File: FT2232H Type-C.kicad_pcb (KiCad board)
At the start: 2 copper layers, 52 x 40 mm, 34 parts, among them J1 CONN_01X20, J2 CONN_01X20, J3 USB_TYPE_C, U1 LD1117S33TR, U3 93CxxB, U4 FT2232H, Y1 12Mhz

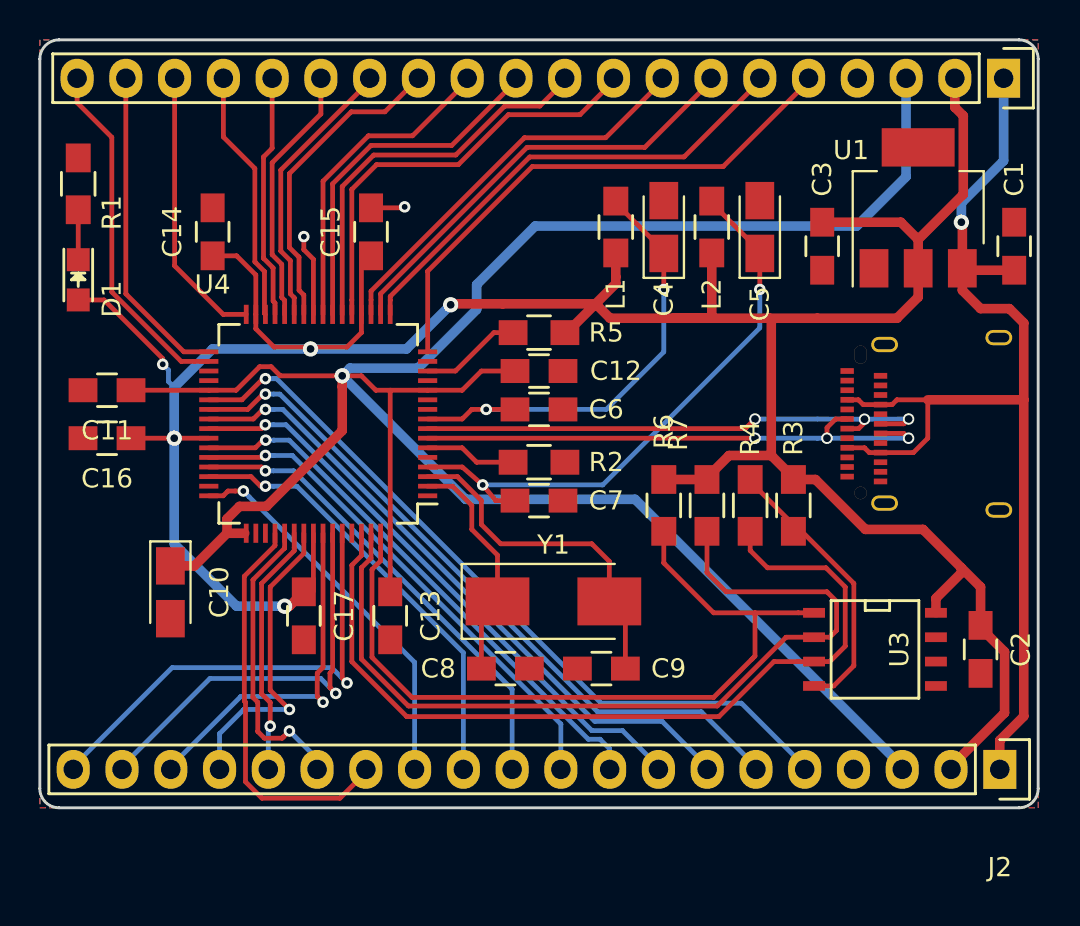
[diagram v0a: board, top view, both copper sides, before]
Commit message: Add silkscreen
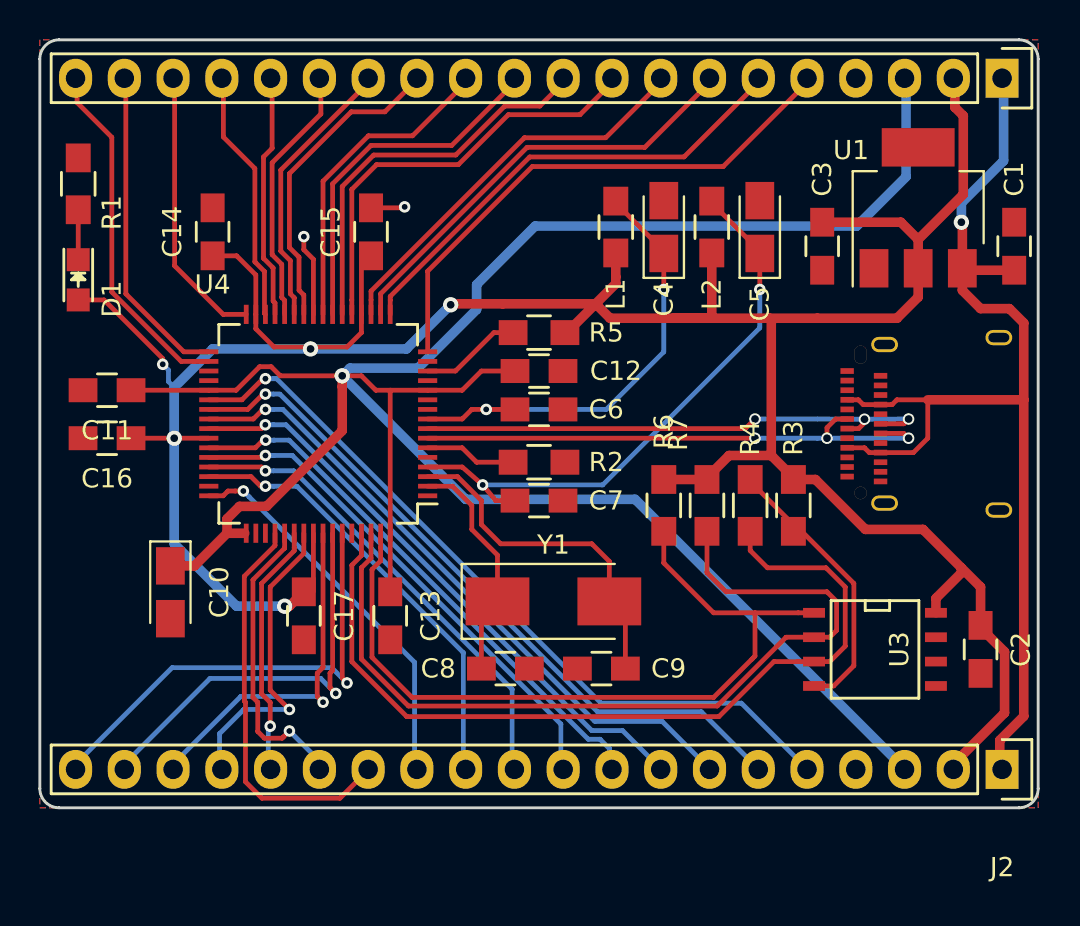
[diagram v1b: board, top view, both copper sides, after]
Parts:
- moved J2 0.12 mm to (198.1, 118.0)
- moved J1 0.08 mm to (198.1, 82.0)
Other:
- rule pad_to_mask_clearance: 0.2 -> 0.1
- board text added: "1.8V"
- board text added: "3.3V"
- board text added: "5.0V"
- board text added: "AC0"
- board text added: "AC1"
- board text added: "AC2"
- board text added: "AC3"
- board text added: "AC4"
- board text added: "AC5"
- board text added: "AC6"
- board text added: "AC7"
- board text added: "AD0"
- board text added: "AD1"
- board text added: "AD2"
- board text added: "AD3"
- board text added: "AD4"
- board text added: "AD5"
- board text added: "AD6"
- board text added: "AD7"
- board text added: "BC0"
- board text added: "BC1"
- board text added: "BC2"
- board text added: "BC3"
- board text added: "BC4"
- board text added: "BC5"
- board text added: "BC6"
- board text added: "BC7"
- board text added: "BD0"
- board text added: "BD1"
- board text added: "BD2"
- board text added: "BD3"
- board text added: "BD4"
- board text added: "BD5"
- board text added: "BD6"
- board text added: "BD7"
- board text added: "FT2232H Type-C Breakout Board Charles-Xavier Roy, Aug 2017"
- board text added: "GND"
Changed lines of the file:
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@@
   (general
     (links 130)
-    (no_connects 64)
+    (no_connects 40)
     (area 147.924999 79.924999 200.075001 120.075001)
     (thickness 1.6)
-    (drawings 8)
+    (drawings 49)
     (tracks 516)
     (zones 0)
@@
     (pad_size 1.524 1.524)
     (pad_drill 0.762)
-    (pad_to_mask_clearance 0.2)
+    (pad_to_mask_clearance 0.1)
+    (solder_mask_min_width 0.32)
     (aux_axis_origin 0 0)
     (visible_elements FFFFFF7F)
     (pcbplotparams
-      (layerselection 0x00030_80000001)
+      (layerselection 0x010f0_80000001)
       (usegerberextensions false)
       (excludeedgelayer true)
@@
       (outputformat 1)
       (mirror false)
-      (drillshape 1)
+      (drillshape 0)
       (scaleselection 1)
-      (outputdirectory ""))
+      (outputdirectory build/))
   )
   (net 0 "")
@@
   )
   (module Socket_Strips:Socket_Strip_Straight_1x20 (layer F.Cu)
-    (at 198.2 82 180)
+    (at 198.12 82 180)
     (descr "Through hole socket strip")
     (tags "socket strip")
@@
   )
   (module Socket_Strips:Socket_Strip_Straight_1x20 (layer F.Cu)
-    (at 198 118 180)
+    (at 198.12 118 180)
     (descr "Through hole socket strip")
     (tags "socket strip")
@@
     )
   )
+  (gr_text "FT2232H Type-C Breakout Board\nCharles-Xavier Roy, Aug 2017" (at 173.75 100.25) (layer B.SilkS)
+    (effects (font (size 1.5 1.5) (thickness 0.3)) (justify mirror))
+  )
+  (gr_text AC0 (at 167.64 83.82 270) (layer B.SilkS)
+    (effects (font (size 1.5 1.5) (thickness 0.3)) (justify right mirror))
+  )
+  (gr_text AD6 (at 172.72 83.82 270) (layer B.SilkS)
+    (effects (font (size 1.5 1.5) (thickness 0.3)) (justify right mirror))
+  )
+  (gr_text AD7 (at 170.18 83.82 270) (layer B.SilkS)
+    (effects (font (size 1.5 1.5) (thickness 0.3)) (justify right mirror))
+  )
+  (gr_text AD4 (at 177.8 83.82 270) (layer B.SilkS)
+    (effects (font (size 1.5 1.5) (thickness 0.3)) (justify right mirror))
+  )
+  (gr_text AD3 (at 180.34 83.82 270) (layer B.SilkS)
+    (effects (font (size 1.5 1.5) (thickness 0.3)) (justify right mirror))
+  )
+  (gr_text AD5 (at 175.26 83.82 270) (layer B.SilkS)
+    (effects (font (size 1.5 1.5) (thickness 0.3)) (justify right mirror))
+  )
+  (gr_text AC7 (at 149.86 83.82 270) (layer B.SilkS)
+    (effects (font (size 1.5 1.5) (thickness 0.3)) (justify right mirror))
+  )
+  (gr_text AC5 (at 154.94 83.82 270) (layer B.SilkS)
+    (effects (font (size 1.5 1.5) (thickness 0.3)) (justify right mirror))
+  )
+  (gr_text AC6 (at 152.4 83.82 270) (layer B.SilkS)
+    (effects (font (size 1.5 1.5) (thickness 0.3)) (justify right mirror))
+  )
+  (gr_text AC1 (at 165.1 83.82 270) (layer B.SilkS)
+    (effects (font (size 1.5 1.5) (thickness 0.3)) (justify right mirror))
+  )
+  (gr_text AC2 (at 162.56 83.82 270) (layer B.SilkS)
+    (effects (font (size 1.5 1.5) (thickness 0.3)) (justify right mirror))
+  )
+  (gr_text AC3 (at 160.02 83.82 270) (layer B.SilkS)
+    (effects (font (size 1.5 1.5) (thickness 0.3)) (justify right mirror))
+  )
+  (gr_text AC4 (at 157.48 83.82 270) (layer B.SilkS)
+    (effects (font (size 1.5 1.5) (thickness 0.3)) (justify right mirror))
+  )
+  (gr_text 5.0V (at 198.12 83.82 270) (layer B.SilkS)
+    (effects (font (size 1.5 1.5) (thickness 0.3)) (justify right mirror))
+  )
+  (gr_text GND (at 190.5 83.82 270) (layer B.SilkS)
+    (effects (font (size 1.5 1.5) (thickness 0.3)) (justify right mirror))
+  )
+  (gr_text AD0 (at 187.96 83.82 270) (layer B.SilkS)
+    (effects (font (size 1.5 1.5) (thickness 0.3)) (justify right mirror))
+  )
+  (gr_text AD2 (at 182.88 83.82 270) (layer B.SilkS)
+    (effects (font (size 1.5 1.5) (thickness 0.3)) (justify right mirror))
+  )
+  (gr_text AD1 (at 185.42 83.82 270) (layer B.SilkS)
+    (effects (font (size 1.5 1.5) (thickness 0.3)) (justify right mirror))
+  )
+  (gr_text 1.8V (at 193.04 83.82 270) (layer B.SilkS)
+    (effects (font (size 1.5 1.5) (thickness 0.3)) (justify right mirror))
+  )
+  (gr_text 3.3V (at 195.58 83.82 270) (layer B.SilkS)
+    (effects (font (size 1.5 1.5) (thickness 0.3)) (justify right mirror))
+  )
+  (gr_text 5.0V (at 198.12 116.34 270) (layer B.SilkS)
+    (effects (font (size 1.5 1.5) (thickness 0.3)) (justify left mirror))
+  )
+  (gr_text 3.3V (at 195.58 116.34 270) (layer B.SilkS)
+    (effects (font (size 1.5 1.5) (thickness 0.3)) (justify left mirror))
+  )
+  (gr_text 1.8V (at 193.04 116.34 270) (layer B.SilkS)
+    (effects (font (size 1.5 1.5) (thickness 0.3)) (justify left mirror))
+  )
+  (gr_text GND (at 190.5 116.34 270) (layer B.SilkS)
+    (effects (font (size 1.5 1.5) (thickness 0.3)) (justify left mirror))
+  )
+  (gr_text BC0 (at 167.64 116.34 270) (layer B.SilkS)
+    (effects (font (size 1.5 1.5) (thickness 0.3)) (justify left mirror))
+  )
+  (gr_text BD0 (at 187.96 116.34 270) (layer B.SilkS)
+    (effects (font (size 1.5 1.5) (thickness 0.3)) (justify left mirror))
+  )
+  (gr_text BD1 (at 185.42 116.34 270) (layer B.SilkS)
+    (effects (font (size 1.5 1.5) (thickness 0.3)) (justify left mirror))
+  )
+  (gr_text BD2 (at 182.88 116.34 270) (layer B.SilkS)
+    (effects (font (size 1.5 1.5) (thickness 0.3)) (justify left mirror))
+  )
+  (gr_text BD3 (at 180.34 116.34 270) (layer B.SilkS)
+    (effects (font (size 1.5 1.5) (thickness 0.3)) (justify left mirror))
+  )
+  (gr_text BD4 (at 177.8 116.34 270) (layer B.SilkS)
+    (effects (font (size 1.5 1.5) (thickness 0.3)) (justify left mirror))
+  )
+  (gr_text BD5 (at 175.26 116.34 270) (layer B.SilkS)
+    (effects (font (size 1.5 1.5) (thickness 0.3)) (justify left mirror))
+  )
+  (gr_text BD6 (at 172.72 116.34 270) (layer B.SilkS)
+    (effects (font (size 1.5 1.5) (thickness 0.3)) (justify left mirror))
+  )
+  (gr_text BD7 (at 170.18 116.34 270) (layer B.SilkS)
+    (effects (font (size 1.5 1.5) (thickness 0.3)) (justify left mirror))
+  )
+  (gr_text BC1 (at 165.1 116.34 270) (layer B.SilkS)
+    (effects (font (size 1.5 1.5) (thickness 0.3)) (justify left mirror))
+  )
+  (gr_text BC2 (at 162.56 116.34 270) (layer B.SilkS)
+    (effects (font (size 1.5 1.5) (thickness 0.3)) (justify left mirror))
+  )
+  (gr_text BC3 (at 160.02 116.34 270) (layer B.SilkS)
+    (effects (font (size 1.5 1.5) (thickness 0.3)) (justify left mirror))
+  )
+  (gr_text BC4 (at 157.48 116.34 270) (layer B.SilkS)
+    (effects (font (size 1.5 1.5) (thickness 0.3)) (justify left mirror))
+  )
+  (gr_text BC5 (at 154.94 116.34 270) (layer B.SilkS)
+    (effects (font (size 1.5 1.5) (thickness 0.3)) (justify left mirror))
+  )
+  (gr_text BC6 (at 152.4 116.34 270) (layer B.SilkS)
+    (effects (font (size 1.5 1.5) (thickness 0.3)) (justify left mirror))
+  )
+  (gr_text BC7 (at 149.86 116.34 270) (layer B.SilkS)
+    (effects (font (size 1.5 1.5) (thickness 0.3)) (justify left mirror))
+  )
   (gr_arc (start 149 119) (end 149 120) (angle 90) (layer Edge.Cuts) (width 0.15))

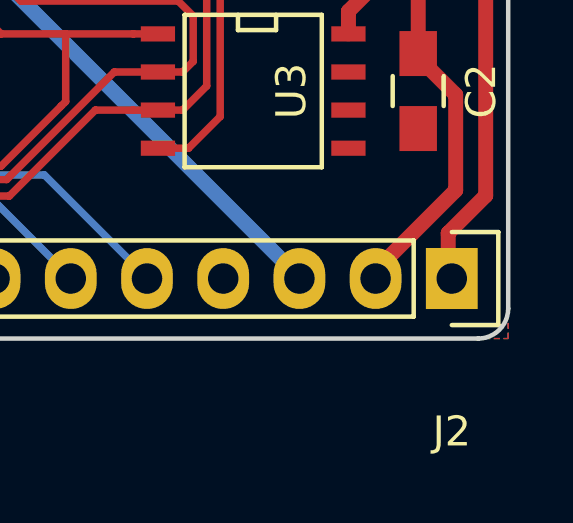
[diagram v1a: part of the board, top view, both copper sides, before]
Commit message: Fit J2 Silkscreen Position
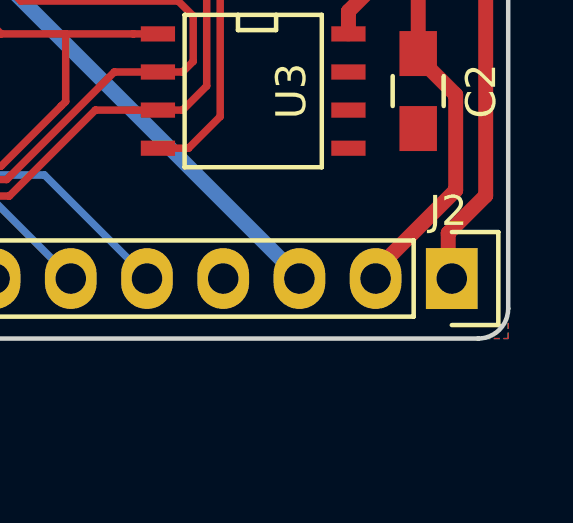
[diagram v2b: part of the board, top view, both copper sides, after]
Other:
- rule solder_mask_min_width: 0.32 -> 0.1
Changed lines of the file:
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@@
   (general
     (links 130)
-    (no_connects 40)
-    (area 147.924999 79.924999 200.075001 120.075001)
+    (no_connects 6)
+    (area 147.275 79.924999 203.153334 124.175)
     (thickness 1.6)
     (drawings 49)
@@
     (pad_drill 0.762)
     (pad_to_mask_clearance 0.1)
-    (solder_mask_min_width 0.32)
+    (solder_mask_min_width 0.1)
     (aux_axis_origin 0 0)
     (visible_elements FFFFFF7F)
@@
     (descr "Through hole socket strip")
     (tags "socket strip")
-    (fp_text reference J2 (at 0 -5.1 180) (layer F.SilkS)
-      (effects (font (size 1 1) (thickness 0.15)))
-    )
+    (fp_text reference J2 (at 0.12 2.25 180) (layer F.SilkS)
+      (effects (font (size 1 1) (thickness 0.15)))
+    )

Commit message: Couple of last minute fixes
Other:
- rule solder_mask_min_width: 0.1 -> 0.4
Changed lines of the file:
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@@
     (links 130)
     (no_connects 6)
-    (area 147.275 79.924999 203.153334 124.175)
+    (area 147.275 79.924999 203.153334 122.175)
     (thickness 1.6)
     (drawings 49)
@@
     (pad_drill 0.762)
     (pad_to_mask_clearance 0.1)
-    (solder_mask_min_width 0.1)
+    (solder_mask_min_width 0.4)
     (aux_axis_origin 0 0)
     (visible_elements FFFFFF7F)
